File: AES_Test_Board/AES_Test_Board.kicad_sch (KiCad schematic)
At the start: 14 parts, among them J1 Conn_02x06_Top_Bottom, J2 Conn_02x06_Top_Bottom, J4 Conn_01x01, J5 Conn_01x01

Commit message: Finished board
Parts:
- removed J4, J5: Conn_01x01, Connector:Banana_Jack_1Pin, symbol Connector_Generic:Conn_01x01
- removed R10, R11, R12, R4, R5, R6, R7, R8, R9: 0, Resistor_SMD:R_0805_2012Metric, symbol Device:R
- added BSY1: BSY, TestPoint:TestPoint_Keystone_5000-5004_Miniature, symbol Connector:TestPoint
- added C1, C4: .1u, Capacitor_SMD:C_0805_2012Metric_Pad1.18x1.45mm_HandSolder, symbol Device:C
- added C10, C2, C5, C7, C8, C9: 1u, Capacitor_SMD:C_0805_2012Metric_Pad1.18x1.45mm_HandSolder, symbol Device:C
- added C3, C6: 10u, Capacitor_SMD:C_0805_2012Metric_Pad1.18x1.45mm_HandSolder, symbol Device:C
- added CLK1: CLK, TestPoint:TestPoint_Keystone_5000-5004_Miniature, symbol Connector:TestPoint
- added CLKOUT1: CLKOUT, TestPoint:TestPoint_Keystone_5000-5004_Miniature, symbol Connector:TestPoint
- added DRDY1: DRDY, TestPoint:TestPoint_Keystone_5000-5004_Miniature, symbol Connector:TestPoint
- added EN1: EN, TestPoint:TestPoint_Keystone_5000-5004_Miniature, symbol Connector:TestPoint
- added KRDY1: KRDY, TestPoint:TestPoint_Keystone_5000-5004_Miniature, symbol Connector:TestPoint
- added RSTN1: RSTN, TestPoint:TestPoint_Keystone_5000-5004_Miniature, symbol Connector:TestPoint
- added SCLK1: SCLK, TestPoint:TestPoint_Keystone_5000-5004_Miniature, symbol Connector:TestPoint
- added SE1: SE, TestPoint:TestPoint_Keystone_5000-5004_Miniature, symbol Connector:TestPoint
- added SI1: SI, TestPoint:TestPoint_Keystone_5000-5004_Miniature, symbol Connector:TestPoint
- added SO1: SO, TestPoint:TestPoint_Keystone_5000-5004_Miniature, symbol Connector:TestPoint
- added SU1: SU, TestPoint:TestPoint_Keystone_5000-5004_Miniature, symbol Connector:TestPoint
- added U2: TLV74010PDBVR, Package_TO_SOT_SMD:SOT-23-5, symbol Regulator_Linear:TLV70012_SOT23-5
- added VDDD1: VDDD, TestPoint:TestPoint_Keystone_5000-5004_Miniature, symbol Connector:TestPoint
- added VDDPST1: VDDPST, TestPoint:TestPoint_Keystone_5000-5004_Miniature, symbol Connector:TestPoint
- added VSS1: VSS, TestPoint:TestPoint_Keystone_5000-5004_Miniature, symbol Connector:TestPoint
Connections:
- net VSSPST is gone; now on net VSS: U1.1 (VSSPST)
- net BSY: now also J1.1 (Pin_1), BSY1.1; no longer J1.10 (Pin_10)
- net CLK: now also J1.8 (Pin_8), U1.46 (AES_CLK), CLK1.1; no longer J2.3 (Pin_3)
- net CLKOUT: now also CLKOUT1.1; no longer J2.4 (Pin_4)
- net DRDY: now also J1.7 (Pin_7), U1.44 (AES_Drdy), DRDY1.1; no longer J2.2 (Pin_2)
- net ENABLE: now also J1.3 (Pin_3), U1.47 (AES_ENABLE), EN1.1; no longer J1.9 (Pin_9)
- net KRDY: now also J1.2 (Pin_2), U1.45 (AES_Krdy), KRDY1.1; no longer J2.1 (Pin_1)
- net RSTN: now also J1.9 (Pin_9), U1.48 (AES_RSTN), RSTN1.1; no longer J1.8 (Pin_8)
- net SCAN_CLK: now also J2.2 (Pin_2), U1.52 (AES_SCAN_CLK), SCLK1.1; no longer J1.4 (Pin_4)
- net SCAN_ENABLE: now also J1.10 (Pin_10), U1.50 (AES_SCAN_ENABLE), SE1.1; no longer J1.2 (Pin_2)
- net SCAN_IN: now also J1.4 (Pin_4), U1.49 (AES_SCAN_IN), SI1.1; no longer J1.1 (Pin_1)
- net SCAN_OUT: now also J2.1 (Pin_1), SO1.1; no longer J1.7 (Pin_7)
- net SCAN_UPDATE: now also J2.3 (Pin_3), U1.53 (AES_SCAN_UPDATE), SU1.1; no longer J1.3 (Pin_3)
- net VDDPST: now also J1.12 (Pin_12), J1.6 (Pin_6), C10.1, C4.1, C5.1, C6.1, C8.1, U2.1 (IN), U2.3 (EN), VDDPST1.1
- net VSS: now also C1.2, C10.2, C2.2, C3.2, C4.2, C5.2, C6.2, C7.2, C8.2, C9.2, U2.2 (GND), VSS1.1
- removed net VDD: J1.12 (Pin_12), J1.6 (Pin_6), U1.55 (VDD0)
- new net VDDD: C1.1, C2.1, C3.1, C7.1, C9.1, U1.55 (VDD0), U2.5 (OUT), VDDD1.1
- no-connect marks 9 -> 10
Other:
- note added: "VDDPST: 3.3V Input for I/O Logic VDDD: 1V Rail that powers AES Internal Logic VDDPOC: VSS: Shared Ground between 2 pins"
- moved on the sheet: U1

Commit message: Emulation Board bitstream works
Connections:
- net VDDPST: now also U1.54 (VDDPOC)
- no-connect marks 10 -> 9
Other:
- note added: "VDDPST: 3.3V Input for I/O Logic VDDD: 1V Rail that powers AES Internal Logic VDDPOC: 3.3V Rail VSS: Shared Ground between 2 pins"
- note removed: "VDDPST: 3.3V Input for I/O Logic VDDD: 1V Rail that powers AES Internal Logic VDDPOC: VSS: Shared Ground between 2 pins"
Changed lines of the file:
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@@
   (no_connect (at 45.085 111.76))
   (no_connect (at 45.085 109.22))
-  (no_connect (at 169.545 78.74))
   (wire (pts (xy 146.05 109.22) (xy 146.685 109.22))
     (stroke (width 0) (type default))
@@
     (stroke (width 0) (type default))
   )
+  (wire (pts (xy 167.005 71.12) (xy 169.545 71.12))
+    (stroke (width 0) (type default))
+  )
   (wire (pts (xy 73.025 140.97) (xy 73.025 146.05))
     (stroke (width 0) (type default))
@@
     (stroke (width 0) (type default))
   )
+  (wire (pts (xy 169.545 71.12) (xy 169.545 78.74))
+    (stroke (width 0) (type default))
+  )
   (wire (pts (xy 57.15 139.7) (xy 57.15 140.97))
     (stroke (width 0) (type default))
@@
     (stroke (width 0) (type default))
   )
-  (text "VDDPST: 3.3V Input for I/O Logic\nVDDD: 1V Rail that powers AES Internal Logic\nVDDPOC: \nVSS: Shared Ground between 2 pins"
+  (text "VDDPST: 3.3V Input for I/O Logic\nVDDD: 1V Rail that powers AES Internal Logic\nVDDPOC: 3.3V Rail\nVSS: Shared Ground between 2 pins"
     (at 66.675 64.77 0)
     (effects (font (size 1.27 1.27)) (justify left bottom))

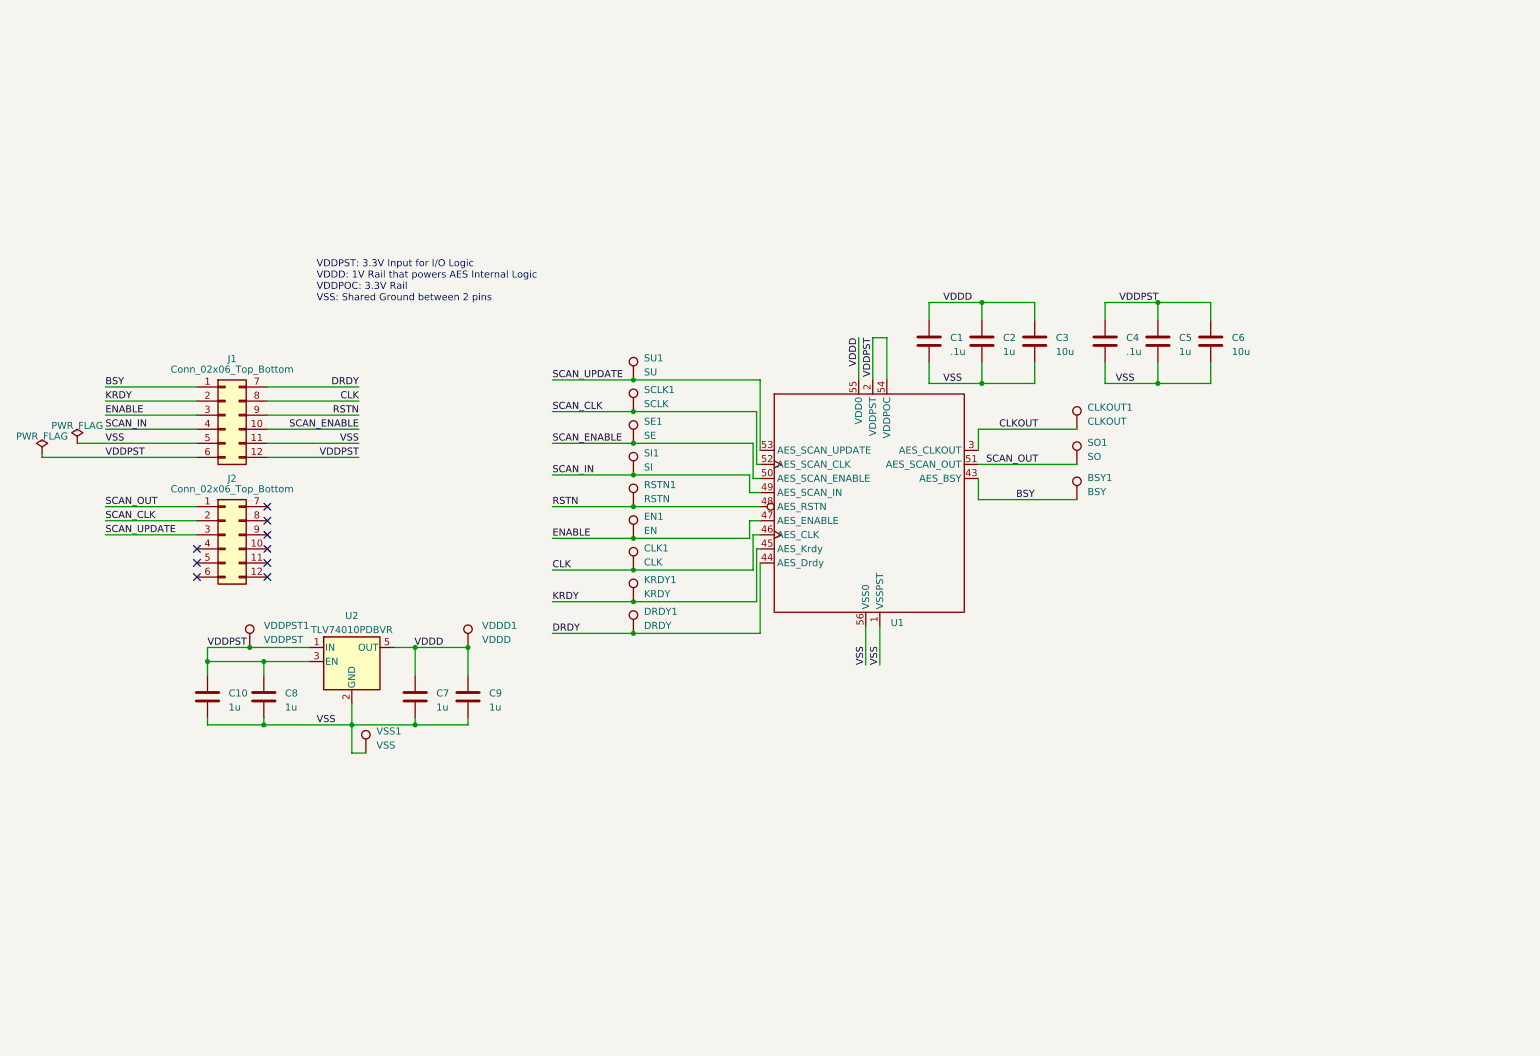
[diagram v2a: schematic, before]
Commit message: Created new vivado project that has both test and emulation synthesizable code within it. Also changed PCB to match professors input
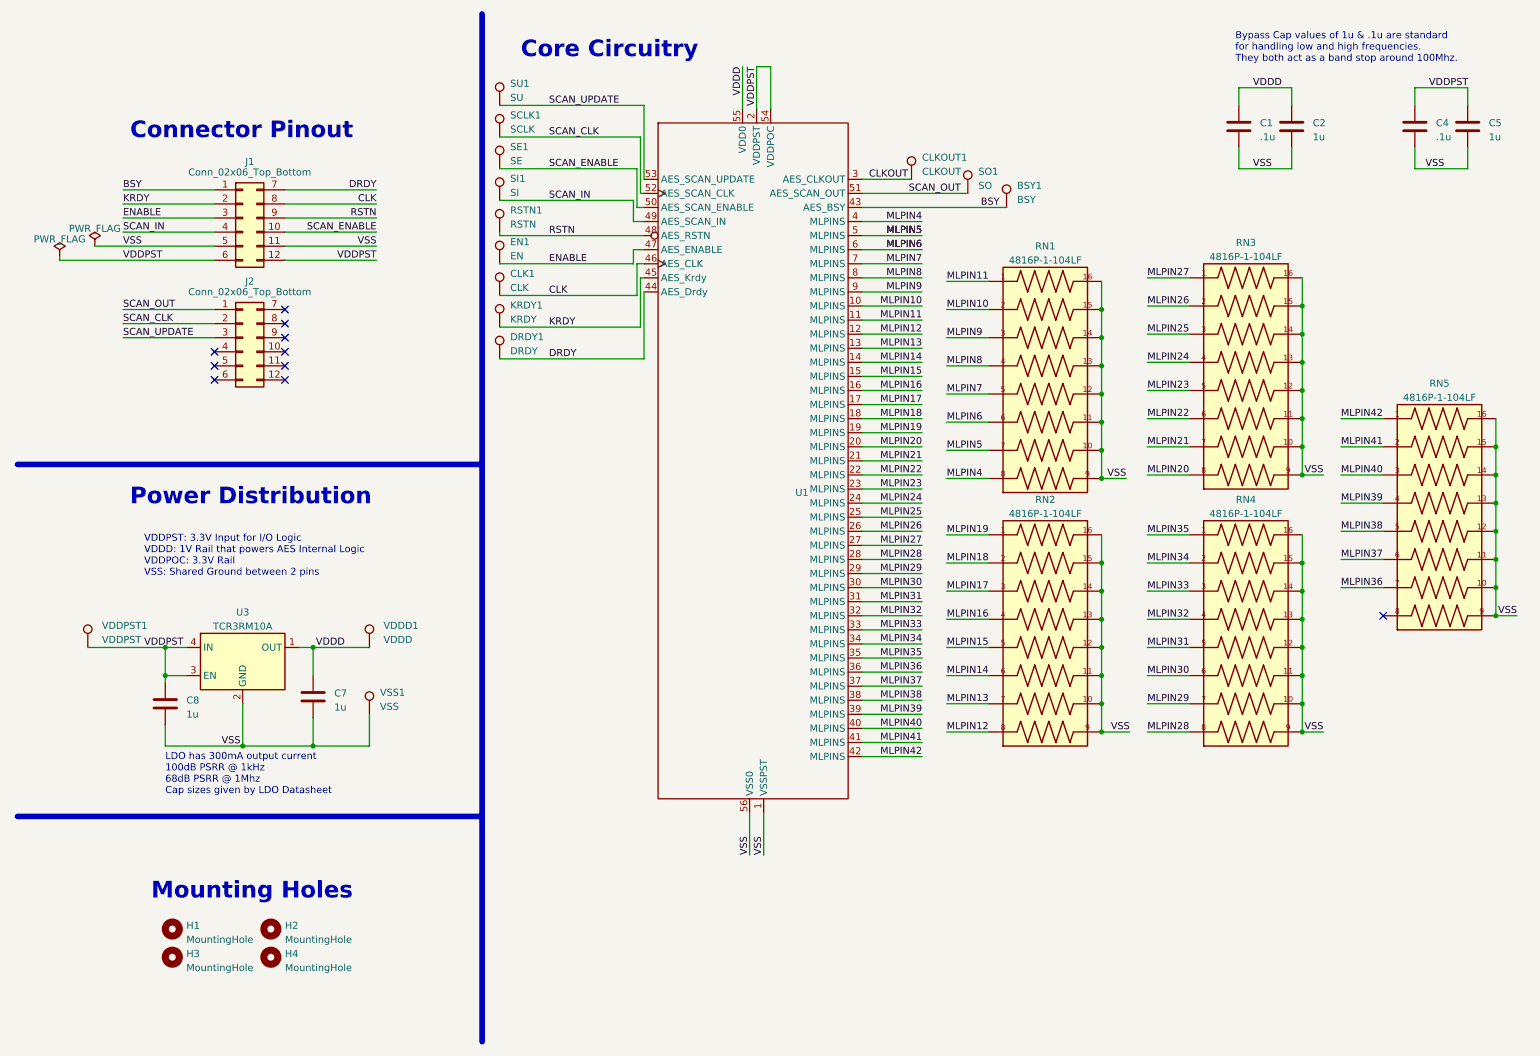
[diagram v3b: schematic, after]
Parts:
- removed C10, C9: 1u, Capacitor_SMD:C_0805_2012Metric_Pad1.18x1.45mm_HandSolder, symbol Device:C
- removed C3, C6: 10u, Capacitor_SMD:C_0805_2012Metric_Pad1.18x1.45mm_HandSolder, symbol Device:C
- removed U2: TLV74010PDBVR, Package_TO_SOT_SMD:SOT-23-5, symbol Regulator_Linear:TLV70012_SOT23-5
- added H1, H2, H3, H4: MountingHole, MountingHole:MountingHole_3.2mm_M3, symbol Mechanical:MountingHole
- added RN1, RN2, RN3, RN4, RN5: 4816P-1-104LF, Connector:SOIC127P762X240-16N, symbol AESCoreTestSym:4816P-1-104LF
- added U3: TCR3RM10A, Package_DFN_QFN:UDFN-4-1EP_1x1mm_P0.65mm_EP0.48x0.48mm, symbol AESCoreTestSym:NCP115AMX120TCG
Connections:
- net VDDD: now also U3.1 (OUT)
- net VDDPST: now also U3.3 (EN), U3.4 (IN)
- net VSS: now also RN1.10, RN1.11, RN1.12, RN1.13, RN1.14, RN1.15, RN1.16, RN1.9, RN2.10, RN2.11, RN2.12, RN2.13, RN2.14, RN2.15, RN2.16, RN2.9, RN3.10, RN3.11, RN3.12, RN3.13, RN3.14, RN3.15, RN3.16, RN3.9, RN4.10, RN4.11, RN4.12, RN4.13, RN4.14, RN4.15, RN4.16, RN4.9, RN5.10, RN5.11, RN5.12, RN5.13, RN5.14, RN5.15, RN5.16, RN5.9, U3.2 (GND), U3.5 (GND)
- new net MLPIN10: RN1.2, U1.10 (MLPINS)
- new net MLPIN11: RN1.1, U1.11 (MLPINS)
- new net MLPIN12: RN2.8, U1.12 (MLPINS)
- new net MLPIN13: RN2.7, U1.13 (MLPINS)
- new net MLPIN14: RN2.6, U1.14 (MLPINS)
- new net MLPIN15: RN2.5, U1.15 (MLPINS)
- new net MLPIN16: RN2.4, U1.16 (MLPINS)
- new net MLPIN17: RN2.3, U1.17 (MLPINS)
- new net MLPIN18: RN2.2, U1.18 (MLPINS)
- new net MLPIN19: RN2.1, U1.19 (MLPINS)
- new net MLPIN20: RN3.8, U1.20 (MLPINS)
- new net MLPIN21: RN3.7, U1.21 (MLPINS)
- new net MLPIN22: RN3.6, U1.22 (MLPINS)
- new net MLPIN23: RN3.5, U1.23 (MLPINS)
- new net MLPIN24: RN3.4, U1.24 (MLPINS)
- new net MLPIN25: RN3.3, U1.25 (MLPINS)
- new net MLPIN26: RN3.2, U1.26 (MLPINS)
- new net MLPIN27: RN3.1, U1.27 (MLPINS)
- new net MLPIN28: RN4.8, U1.28 (MLPINS)
- new net MLPIN29: RN4.7, U1.29 (MLPINS)
- new net MLPIN30: RN4.6, U1.30 (MLPINS)
- new net MLPIN31: RN4.5, U1.31 (MLPINS)
- new net MLPIN32: RN4.4, U1.32 (MLPINS)
- new net MLPIN33: RN4.3, U1.33 (MLPINS)
- new net MLPIN34: RN4.2, U1.34 (MLPINS)
- new net MLPIN35: RN4.1, U1.35 (MLPINS)
- new net MLPIN36: RN5.7, U1.36 (MLPINS)
- new net MLPIN37: RN5.6, U1.37 (MLPINS)
- new net MLPIN38: RN5.5, U1.38 (MLPINS)
- new net MLPIN39: RN5.4, U1.39 (MLPINS)
- new net MLPIN4: RN1.8, U1.4 (MLPINS)
- new net MLPIN40: RN5.3, U1.40 (MLPINS)
- new net MLPIN41: RN5.2, U1.41 (MLPINS)
- new net MLPIN42: RN5.1, U1.42 (MLPINS)
- new net MLPIN5: RN1.7, U1.5 (MLPINS)
- new net MLPIN6: RN1.6, U1.6 (MLPINS)
- new net MLPIN7: RN1.5, U1.7 (MLPINS)
- new net MLPIN8: RN1.4, U1.8 (MLPINS)
- new net MLPIN9: RN1.3, U1.9 (MLPINS)
- no-connect marks 9 -> 10
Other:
- note added: "Bypass Cap values of 1u & .1u are standard for handling low and high frequencies. They both act as a band stop around 100Mhz."
- note added: "Connector Pinout"
- note added: "Core Circuitry"
- note added: "LDO has 300mA output current 100dB PSRR @ 1kHz 68dB PSRR @ 1Mhz Cap sizes given by LDO Datasheet"
- note added: "Mounting Holes"
- note added: "Power Distribution"
- moved on the sheet: BSY1, C1, C2, C4, C5, C7, C8, CLK1, CLKOUT1, DRDY1, EN1, J1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
